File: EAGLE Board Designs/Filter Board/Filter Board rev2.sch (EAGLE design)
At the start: 96 parts, among them J4 CONNECTOR-40__, J5 CONNECTOR-40__, U10 MAX7400, U11 MAX7400, U19 MAX7400, U20 MAX7400, U21 MAX7400, U22 MAX7400, U23 MAX7400, U24 MAX7400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

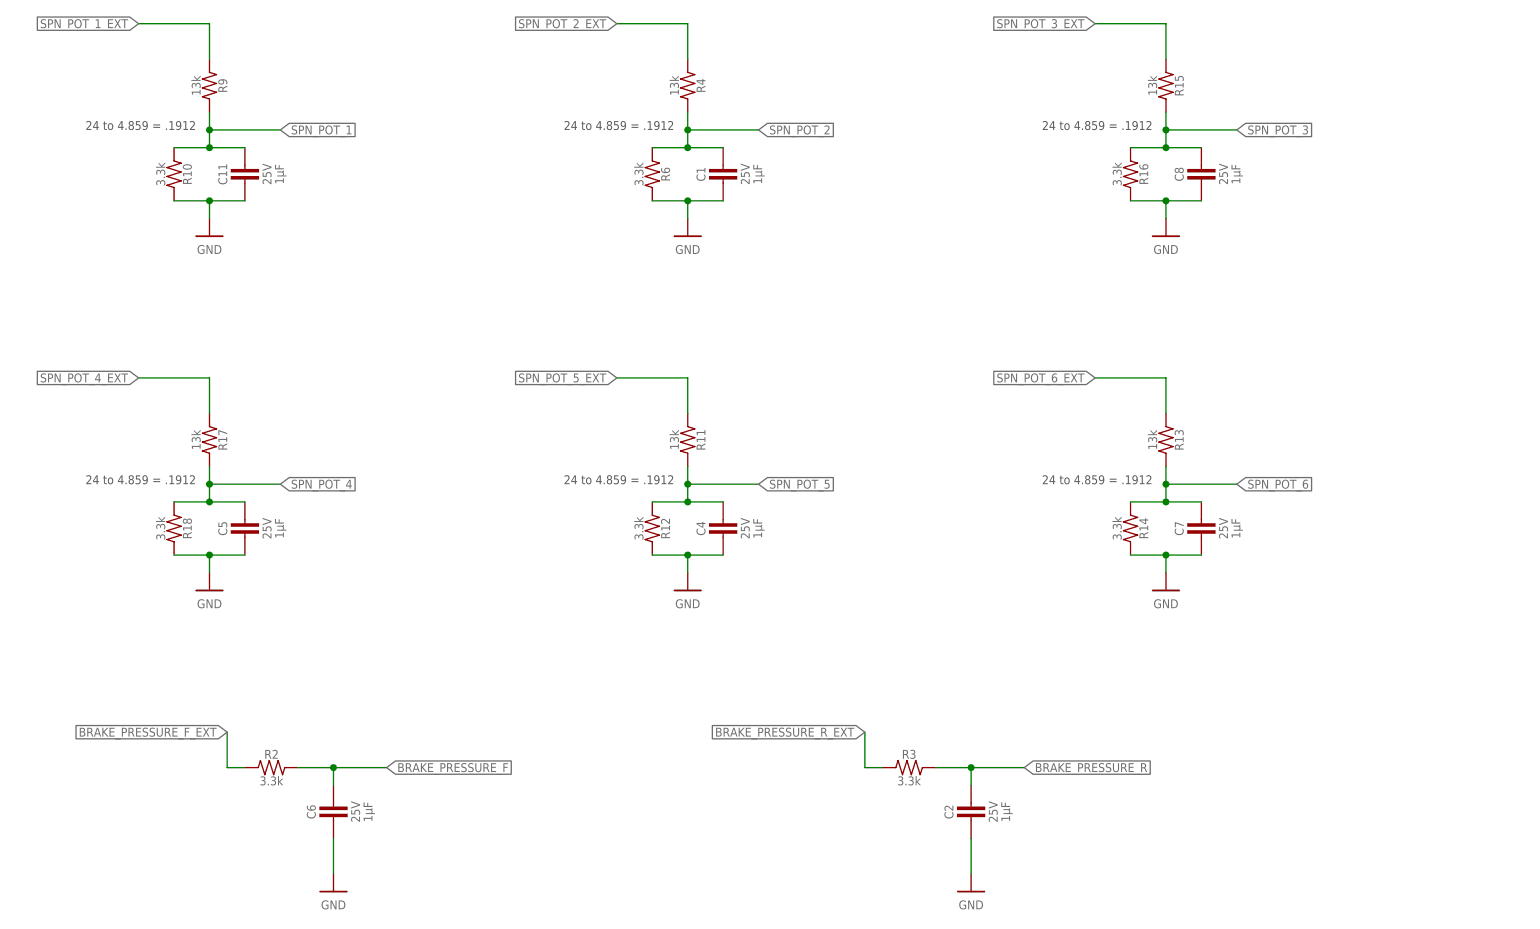
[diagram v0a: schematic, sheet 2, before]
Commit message: updated passive filters and routing
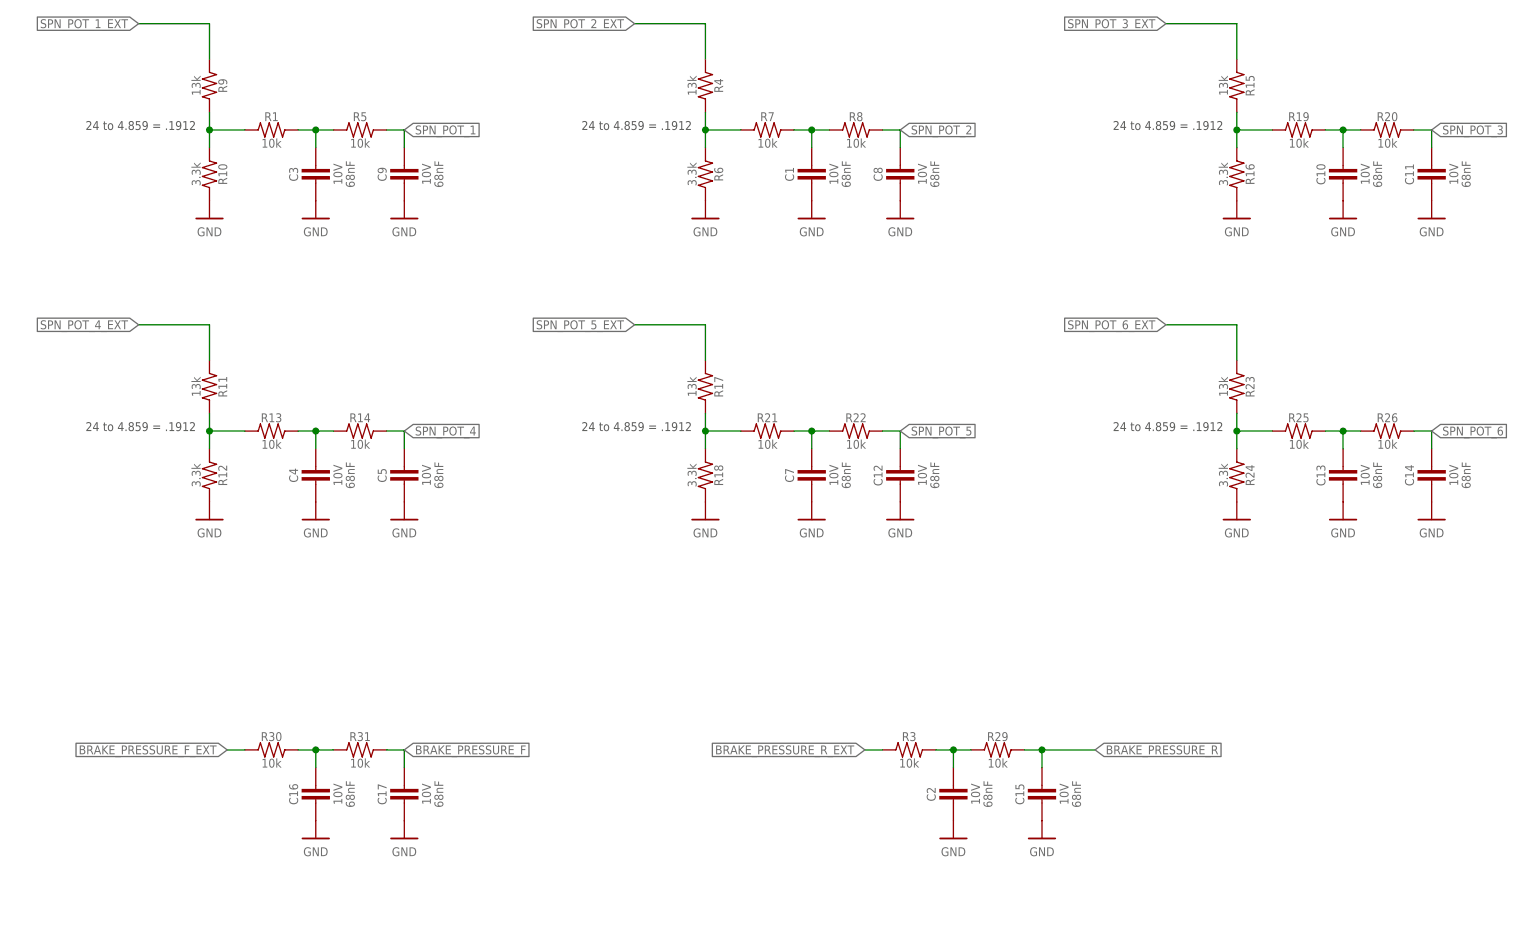
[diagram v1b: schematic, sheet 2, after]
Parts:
- removed C6: CAPACITOR_0603_25V_1UF, HyTechDevices:CAPACITOR_0603_25V_1UF
- removed R2: RESISTOR_0603_3.3K, HyTechDevices:RESISTOR_0603_3.3K
- added C10, C12, C13, C14, C15, C16, C17, C3, C9: CAPACITOR_0603_10V_68NF, HyTechDevices:CAPACITOR_0603_10V_68NF
- added R1, R19, R20, R21, R22, R25, R26, R29, R30, R31, R5, R7, R8: RESISTOR_0603_10K, HyTechDevices:RESISTOR_0603_10K
- added R23: RESISTOR_0603_13K, HyTechDevices:RESISTOR_0603_13K
- added R24: RESISTOR_0603_3.3K, HyTechDevices:RESISTOR_0603_3.3K
- C1, C11, C2, C4, C5, C7, C8: value CAPACITOR_0603_25V_1UF -> CAPACITOR_0603_10V_68NF; device HyTechDevices:CAPACITOR_0603_25V_1UF -> HyTechDevices:CAPACITOR_0603_10V_68NF
- R13: value RESISTOR_0603_13K -> RESISTOR_0603_10K; device HyTechDevices:RESISTOR_0603_13K -> HyTechDevices:RESISTOR_0603_10K
- R14, R3: value RESISTOR_0603_3.3K -> RESISTOR_0603_10K; device HyTechDevices:RESISTOR_0603_3.3K -> HyTechDevices:RESISTOR_0603_10K
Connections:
- new net N$10: R11.2, R12.1, R13.1
- new net N$11: C7.1, R21.2, R22.1
- new net N$12: R17.2, R18.1, R21.1
- new net N$25: C13.1, R25.2, R26.1
- new net N$26: R23.2, R24.1, R25.1
- new net N$27: C2.1, R29.1, R3.2
- new net N$28: C16.1, R30.2, R31.1
- new net N$3: C3.1, R1.2, R5.1
- new net N$4: C1.1, R7.2, R8.1
- new net N$5: R1.1, R10.1, R9.2
- new net N$6: R4.2, R6.1, R7.1
- new net N$7: C10.1, R19.2, R20.1
- new net N$8: R15.2, R16.1, R19.1
- new net N$9: C4.1, R13.2, R14.1
- net BRAKE_PRESSURE_F: now also C17.1, R31.2; no longer C6.1, R2.2
- net BRAKE_PRESSURE_F_EXT: now also R30.1; no longer R2.1
- net BRAKE_PRESSURE_R: now also C15.1, R29.2; no longer C2.1, R3.2
- net GND: now also C10.2, C12.2, C13.2, C14.2, C15.2, C16.2, C17.2, C3.2, C9.2, R24.2; no longer C6.2, R14.2
- net SPN_POT_1: now also C9.1, R5.2; no longer C11.1, R10.1, R9.2
- net SPN_POT_2: now also C8.1, R8.2; no longer C1.1, R4.2, R6.1
- net SPN_POT_3: now also C11.1, R20.2; no longer C8.1, R15.2, R16.1
- net SPN_POT_4: now also R14.2; no longer R17.2, R18.1
- net SPN_POT_4_EXT: now also R11.1; no longer R17.1
- net SPN_POT_5: now also C12.1, R22.2; no longer C4.1, R11.2, R12.1
- net SPN_POT_5_EXT: now also R17.1; no longer R11.1
- net SPN_POT_6: now also C14.1, R26.2; no longer C7.1, R13.2, R14.1
- net SPN_POT_6_EXT: now also R23.1; no longer R13.1
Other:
- moved on the sheet: C1, C11, C2, C4, C5, C7, C8, R10, R11, R12, R13, R14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
